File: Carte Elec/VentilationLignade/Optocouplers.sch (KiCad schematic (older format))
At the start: 0 parts

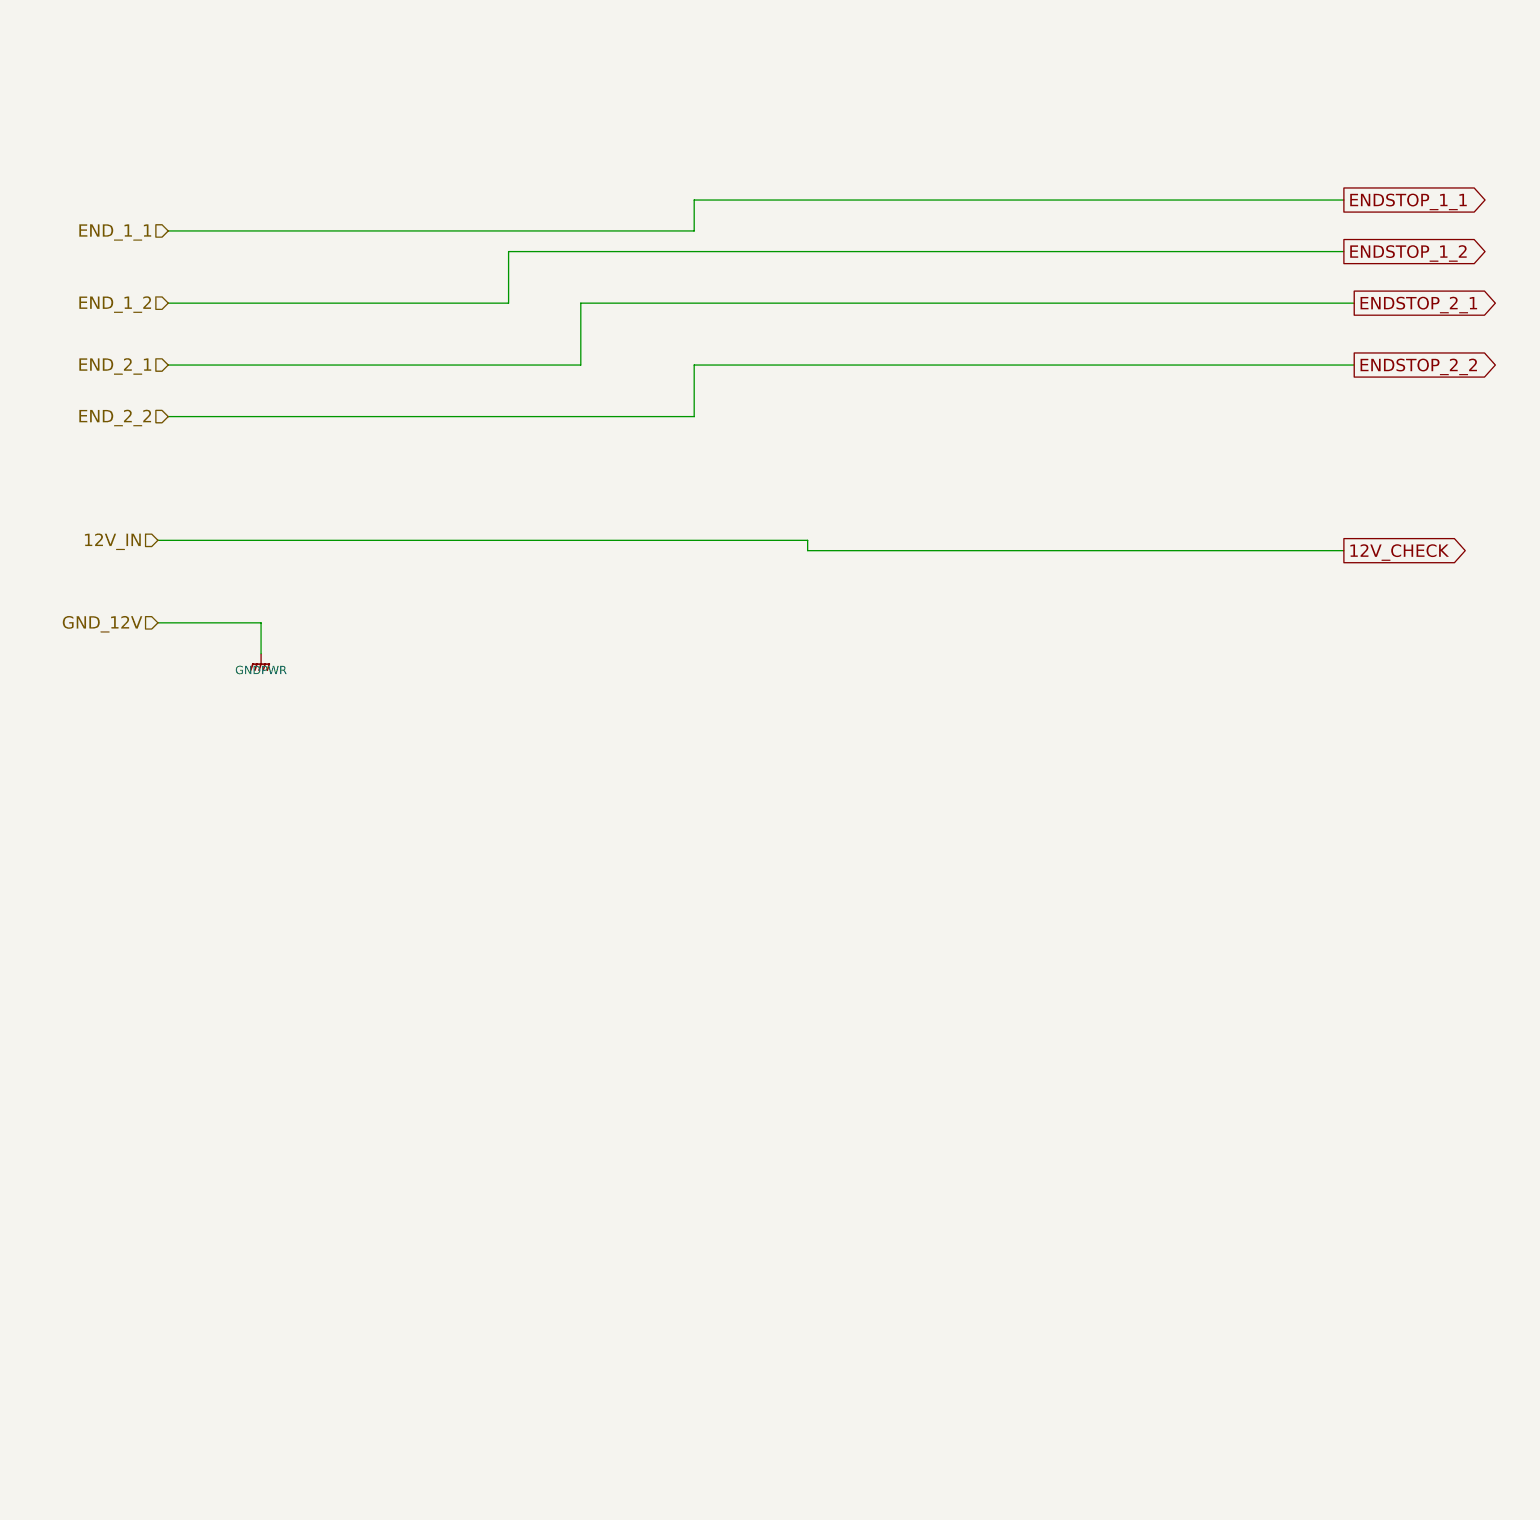
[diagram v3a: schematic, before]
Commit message: Reprise de carte  : Suppression MAX232, pour avoir la place de mettre les MOC207
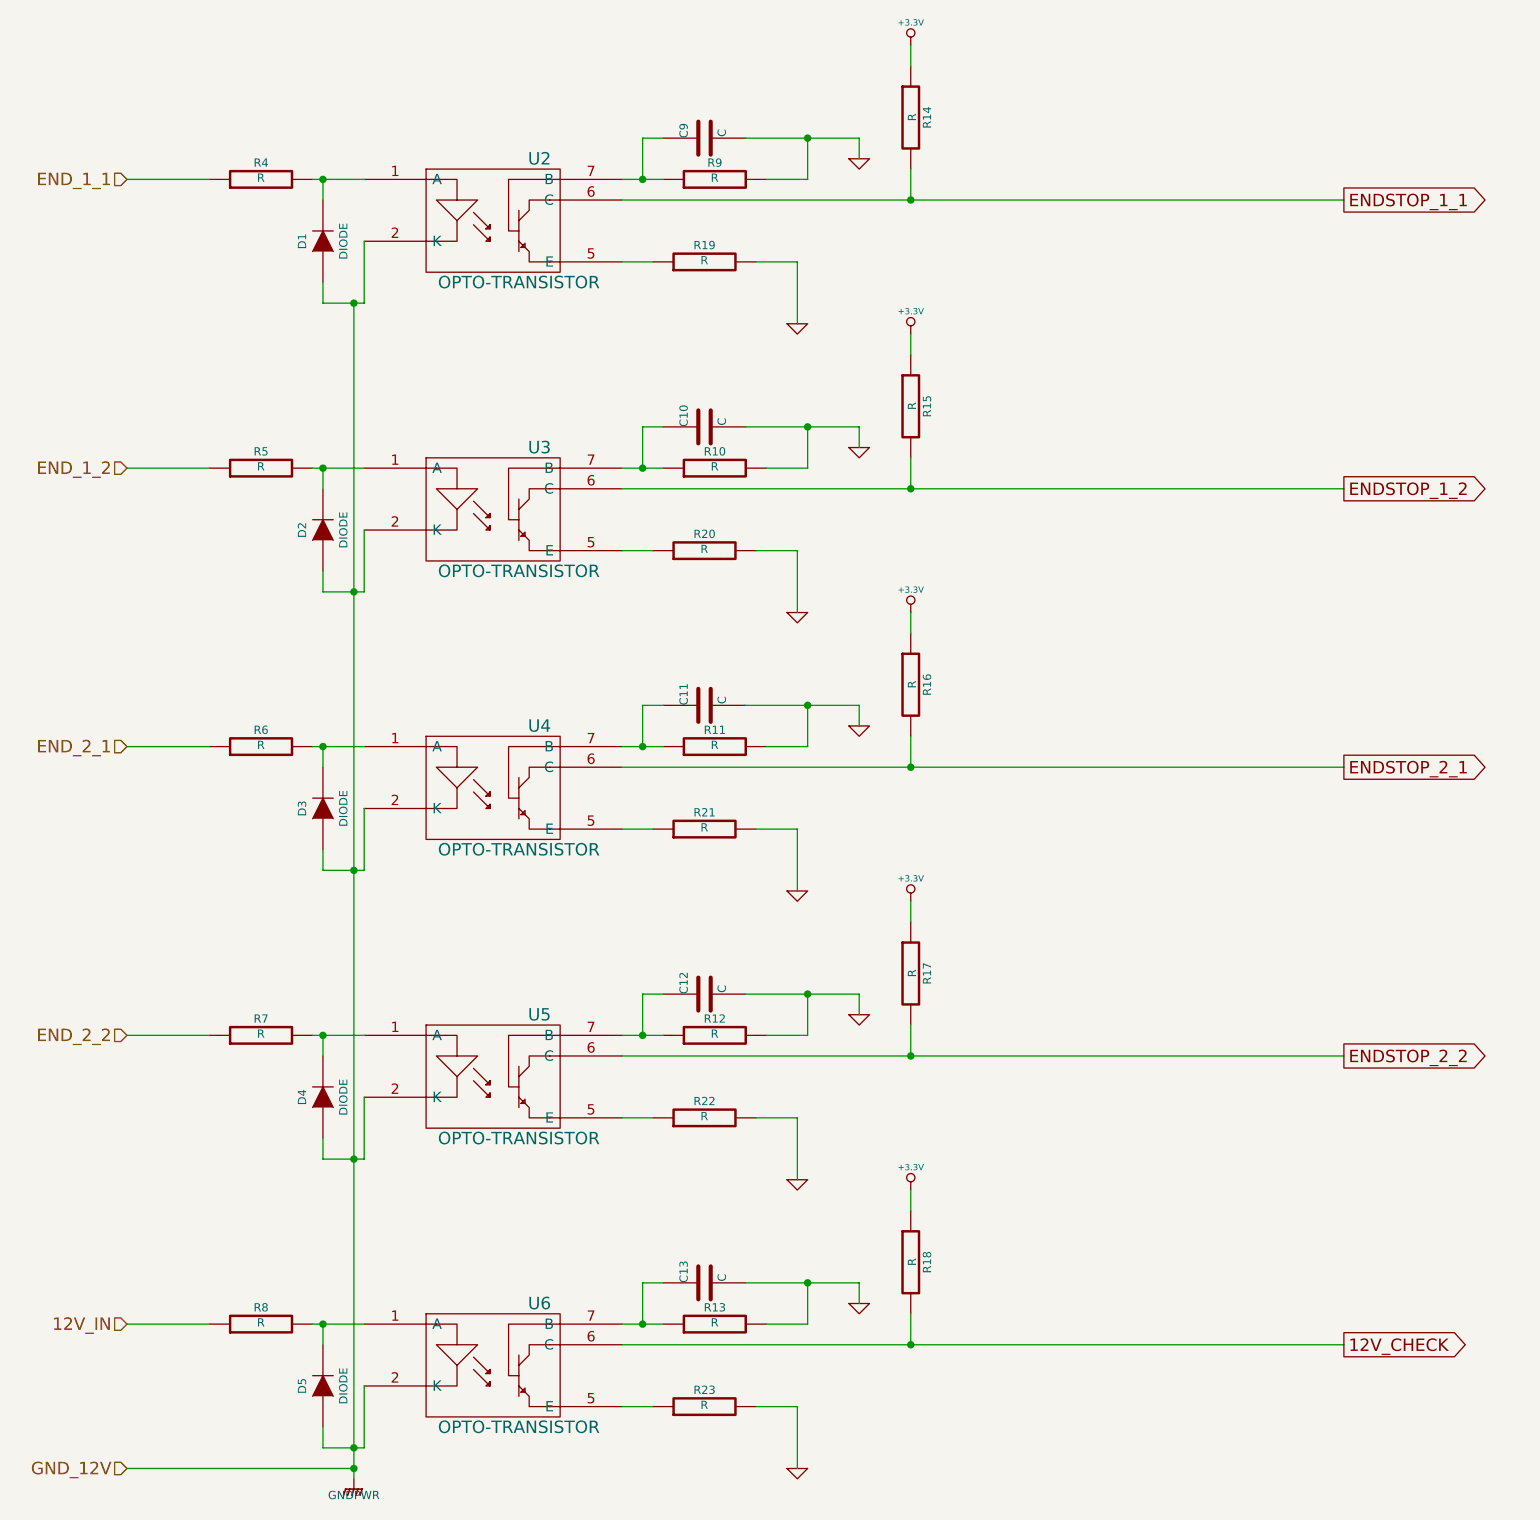
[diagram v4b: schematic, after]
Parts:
- added C10, C11, C12, C13, C9: C, ~, symbol C
- added D1, D2, D3, D4, D5: DIODE, ~, symbol DIODE
- added R10, R11, R12, R13, R14, R15, R16, R17, R18, R19, R20, R21, R22, R23, R4, R5, R6, R7, R8, R9: R, ~, symbol R
- added U2, U3, U4, U5, U6: OPTO-TRANSISTOR, ~, symbol OPTO-TRANSISTOR
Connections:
- net 12V_CHECK: now also R18.2, U6.6 (C)
- net ENDSTOP_1_1: now also R14.2, U2.6 (C)
- net ENDSTOP_1_2: now also R15.2, U3.6 (C)
- net ENDSTOP_2_1: now also R16.2, U4.6 (C)
- net ENDSTOP_2_2: now also R17.2, U5.6 (C)
- net GNDPWR: now also D1.1 (A), D2.1 (A), D3.1 (A), D4.1 (A), D5.1 (A), U2.2 (K), U3.2 (K), U4.2 (K), U5.2 (K), U6.2 (K)
- new net: D1.2 (K), R4.2, U2.1 (A)
- new net: R19.1, U2.5 (E)
- new net: C9.1, R9.1, U2.7 (B)
- new net: D2.2 (K), R5.2, U3.1 (A)
- new net: R20.1, U3.5 (E)
- new net: C10.1, R10.1, U3.7 (B)
- new net: D3.2 (K), R6.2, U4.1 (A)
- new net: R21.1, U4.5 (E)
- new net: C11.1, R11.1, U4.7 (B)
- new net: D4.2 (K), R7.2, U5.1 (A)
- new net: R22.1, U5.5 (E)
- new net: C12.1, R12.1, U5.7 (B)
- new net: D5.2 (K), R8.2, U6.1 (A)
- new net: R23.1, U6.5 (E)
- new net: C13.1, R13.1, U6.7 (B)
- new net +3.3V: R14.1, R15.1, R16.1, R17.1, R18.1
- new net 12V_IN: R8.1
- new net END_1_1: R4.1
- new net END_1_2: R5.1
- new net END_2_1: R6.1
- new net END_2_2: R7.1
- new net GND: C10.2, C11.2, C12.2, C13.2, C9.2, R10.2, R11.2, R12.2, R13.2, R19.2, R20.2, R21.2, R22.2, R23.2, R9.2

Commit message: Modification carte pour utiliser thermistors et real time clock.
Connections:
- no-connect marks 0 -> 5
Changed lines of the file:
@@
 Sheet 2 2
 Title ""
-Date "13 sep 2015"
+Date "1 oct 2015"
 Rev ""
 Comp ""
@@
 $EndComp
 $Comp
-L GND #PWR046
+L GND #PWR043
 U 1 1 55F3F5C0
 P 4650 2050
-F 0 "#PWR046" H 4650 2050 30  0001 C CNN
+F 0 "#PWR043" H 4650 2050 30  0001 C CNN
 F 1 "GND" H 4650 1980 30  0001 C CNN
 F 2 "" H 4650 2050 60  0000 C CNN
@@
 $EndComp
 $Comp
-L GND #PWR047
+L GND #PWR044
 U 1 1 55F3F5CF
 P 4950 1250
-F 0 "#PWR047" H 4950 1250 30  0001 C CNN
+F 0 "#PWR044" H 4950 1250 30  0001 C CNN
 F 1 "GND" H 4950 1180 30  0001 C CNN
 F 2 "" H 4950 1250 60  0000 C CNN
@@
 $EndComp
 $Comp
-L +3.3V #PWR048
+L +3.3V #PWR045
 U 1 1 55F3F634
 P 5200 700
-F 0 "#PWR048" H 5200 660 30  0001 C CNN
+F 0 "#PWR045" H 5200 660 30  0001 C CNN
 F 1 "+3.3V" H 5200 810 30  0000 C CNN
 F 2 "" H 5200 700 60  0000 C CNN
@@
 $EndComp
 $Comp
-L GND #PWR049
+L GND #PWR046
 U 1 1 55F3F692
 P 4650 3450
-F 0 "#PWR049" H 4650 3450 30  0001 C CNN
+F 0 "#PWR046" H 4650 3450 30  0001 C CNN
 F 1 "GND" H 4650 3380 30  0001 C CNN
 F 2 "" H 4650 3450 60  0000 C CNN
@@
 $EndComp
 $Comp
-L GND #PWR050
+L GND #PWR047
 U 1 1 55F3F698
 P 4950 2650
-F 0 "#PWR050" H 4950 2650 30  0001 C CNN
+F 0 "#PWR047" H 4950 2650 30  0001 C CNN
 F 1 "GND" H 4950 2580 30  0001 C CNN
 F 2 "" H 4950 2650 60  0000 C CNN
@@
 $EndComp
 $Comp
-L +3.3V #PWR051
+L +3.3V #PWR048
 U 1 1 55F3F6AF
 P 5200 2100
-F 0 "#PWR051" H 5200 2060 30  0001 C CNN
+F 0 "#PWR048" H 5200 2060 30  0001 C CNN
 F 1 "+3.3V" H 5200 2210 30  0000 C CNN
 F 2 "" H 5200 2100 60  0000 C CNN
@@
 $EndComp
 $Comp
-L GND #PWR052
+L GND #PWR049
 U 1 1 55F3F6DF
 P 4650 4800
-F 0 "#PWR052" H 4650 4800 30  0001 C CNN
+F 0 "#PWR049" H 4650 4800 30  0001 C CNN
 F 1 "GND" H 4650 4730 30  0001 C CNN
 F 2 "" H 4650 4800 60  0000 C CNN
@@
 $EndComp
 $Comp
-L GND #PWR053
+L GND #PWR050
 U 1 1 55F3F6E5
 P 4950 4000
-F 0 "#PWR053" H 4950 4000 30  0001 C CNN
+F 0 "#PWR050" H 4950 4000 30  0001 C CNN
 F 1 "GND" H 4950 3930 30  0001 C CNN
 F 2 "" H 4950 4000 60  0000 C CNN
@@
 $EndComp
 $Comp
-L +3.3V #PWR054
+L +3.3V #PWR051
 U 1 1 55F3F6FC
 P 5200 3450
-F 0 "#PWR054" H 5200 3410 30  0001 C CNN
+F 0 "#PWR051" H 5200 3410 30  0001 C CNN
 F 1 "+3.3V" H 5200 3560 30  0000 C CNN
 F 2 "" H 5200 3450 60  0000 C CNN
@@
 $EndComp
 $Comp
-L GND #PWR055
+L GND #PWR052
 U 1 1 55F3F72C
 P 4650 6200
-F 0 "#PWR055" H 4650 6200 30  0001 C CNN
+F 0 "#PWR052" H 4650 6200 30  0001 C CNN
 F 1 "GND" H 4650 6130 30  0001 C CNN
 F 2 "" H 4650 6200 60  0000 C CNN
@@
 $EndComp
 $Comp
-L GND #PWR056
+L GND #PWR053
 U 1 1 55F3F732
 P 4950 5400
-F 0 "#PWR056" H 4950 5400 30  0001 C CNN
+F 0 "#PWR053" H 4950 5400 30  0001 C CNN
 F 1 "GND" H 4950 5330 30  0001 C CNN
 F 2 "" H 4950 5400 60  0000 C CNN
@@
 $EndComp
 $Comp
-L +3.3V #PWR057
+L +3.3V #PWR054
 U 1 1 55F3F749
 P 5200 4850
-F 0 "#PWR057" H 5200 4810 30  0001 C CNN
+F 0 "#PWR054" H 5200 4810 30  0001 C CNN
 F 1 "+3.3V" H 5200 4960 30  0000 C CNN
 F 2 "" H 5200 4850 60  0000 C CNN
@@
 $EndComp
 $Comp
-L GND #PWR058
+L GND #PWR055
 U 1 1 55F3F780
 P 4650 7600
-F 0 "#PWR058" H 4650 7600 30  0001 C CNN
+F 0 "#PWR055" H 4650 7600 30  0001 C CNN
 F 1 "GND" H 4650 7530 30  0001 C CNN
 F 2 "" H 4650 7600 60  0000 C CNN
@@
 $EndComp
 $Comp
-L GND #PWR059
+L GND #PWR056
 U 1 1 55F3F786
 P 4950 6800
-F 0 "#PWR059" H 4950 6800 30  0001 C CNN
+F 0 "#PWR056" H 4950 6800 30  0001 C CNN
 F 1 "GND" H 4950 6730 30  0001 C CNN
 F 2 "" H 4950 6800 60  0000 C CNN
@@
 $EndComp
 $Comp
-L +3.3V #PWR060
+L +3.3V #PWR057
 U 1 1 55F3F79D
 P 5200 6250
-F 0 "#PWR060" H 5200 6210 30  0001 C CNN
+F 0 "#PWR057" H 5200 6210 30  0001 C CNN
 F 1 "+3.3V" H 5200 6360 30  0000 C CNN
 F 2 "" H 5200 6250 60  0000 C CNN
@@
 Connection ~ 2500 7500
 $Comp
-L GNDPWR #PWR061
+L GNDPWR #PWR058
 U 1 1 55F3FD73
 P 2500 7650
-F 0 "#PWR061" H 2500 7700 40  0001 C CNN
+F 0 "#PWR058" H 2500 7700 40  0001 C CNN
 F 1 "GNDPWR" H 2500 7570 40  0000 C CNN
 F 2 "" H 2500 7650 60  0000 C CNN
@@
 Wire Wire Line
 	3950 7300 3800 7300
+NoConn ~ 2850 5900
+NoConn ~ 2850 7300
+NoConn ~ 2850 4500
+NoConn ~ 2850 1750
+NoConn ~ 2850 3150
 $EndSCHEMATC

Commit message: Changement des boitiers en cours de reroutage
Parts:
- C10, C11, C12, C13, C9: footprint ~ -> Capacitors_SMD:C_0805_HandSoldering; symbol C -> C-RESCUE-VentilationLignade
- D1, D2, D3, D4, D5: footprint ~ -> TO_SOT_Packages_SMD:SOT-23
- R10, R11, R12, R13, R14, R15, R16, R17, R18, R19, R20, R21, R22, R23, R4, R5, R6, R7, R8, R9: footprint ~ -> Resistors_SMD:R_1206_HandSoldering; symbol R -> R-RESCUE-VentilationLignade
- U2, U3, U4, U5, U6: footprint ~ -> SMD_Packages:SOIC-8-N; symbol OPTO-TRANSISTOR -> OPTO-TRANSISTOR-RESCUE-VentilationLignade
